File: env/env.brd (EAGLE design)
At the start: 86.3 x 107.6 mm, 103 parts, among them IC1 DG403DJD, IC2 OPA4130U, IC3 4001D, IC4 OPA2134D, IC5 OPA4130U, Q1 BC847ALT1SMD, Q2 BC857ALT1SMD, Q3 BC847ALT1SMD, Q4 BC847ALT1SMD, X1 2516-

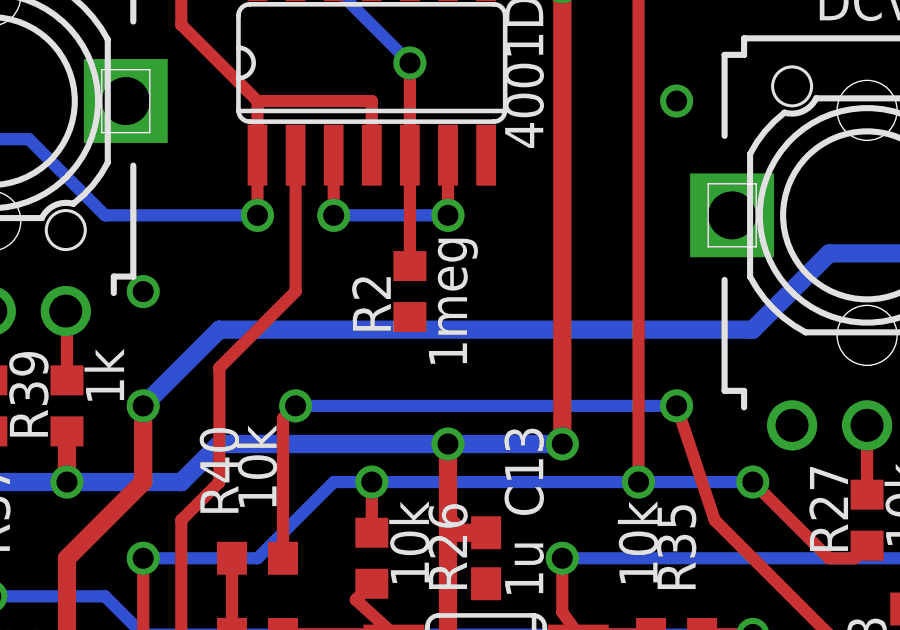
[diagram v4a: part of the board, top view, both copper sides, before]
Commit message: Added env front panel.  Fixed a resistor in the env.
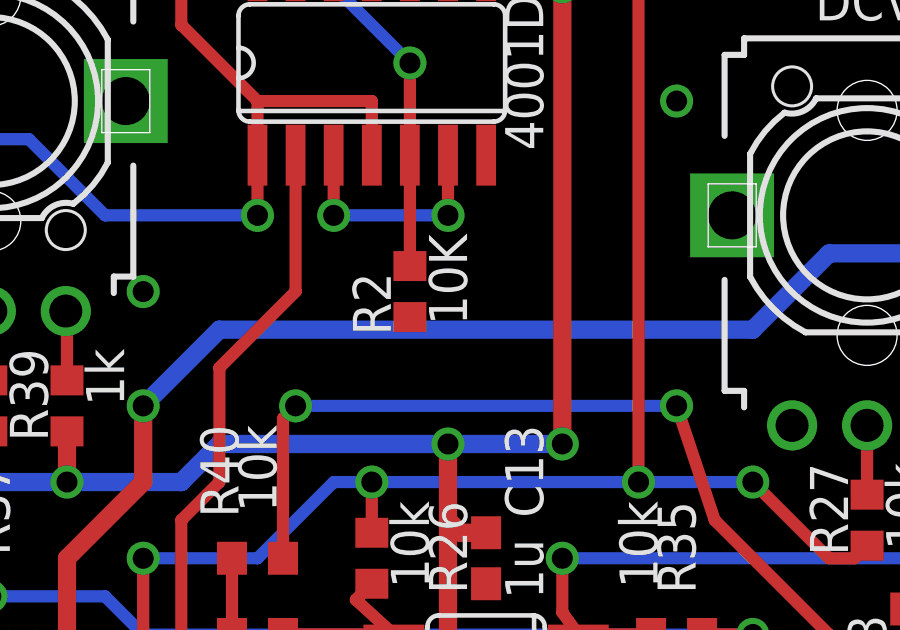
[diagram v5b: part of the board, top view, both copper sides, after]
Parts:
- R2: value 1meg -> 10K
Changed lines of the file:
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@@
 <?xml version="1.0" encoding="utf-8"?>
 <!DOCTYPE eagle SYSTEM "eagle.dtd">
-<eagle version="7.2.0">
+<eagle version="7.6.0">
 <drawing>
 <settings>
@@
 <attribute name="VALUE" x="36.195" y="12.065" size="1.27" layer="21" font="vector" ratio="15" rot="R270"/>
 </element>
-<element name="R2" library="dan" package="R0603" value="1meg" x="57.15" y="64.77" smashed="yes" rot="R90">
+<element name="R2" library="dan" package="R0603" value="10K" x="57.15" y="64.77" smashed="yes" rot="R90">
 <attribute name="NAME" x="55.245" y="65.405" size="1.27" layer="21" font="vector" ratio="15" rot="R270"/>
 <attribute name="VALUE" x="57.785" y="66.675" size="1.27" layer="21" font="vector" ratio="15" rot="R270"/>
